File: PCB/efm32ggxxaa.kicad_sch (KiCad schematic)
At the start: 8 parts, among them U5 EFM32GG11B420F2048GQ100

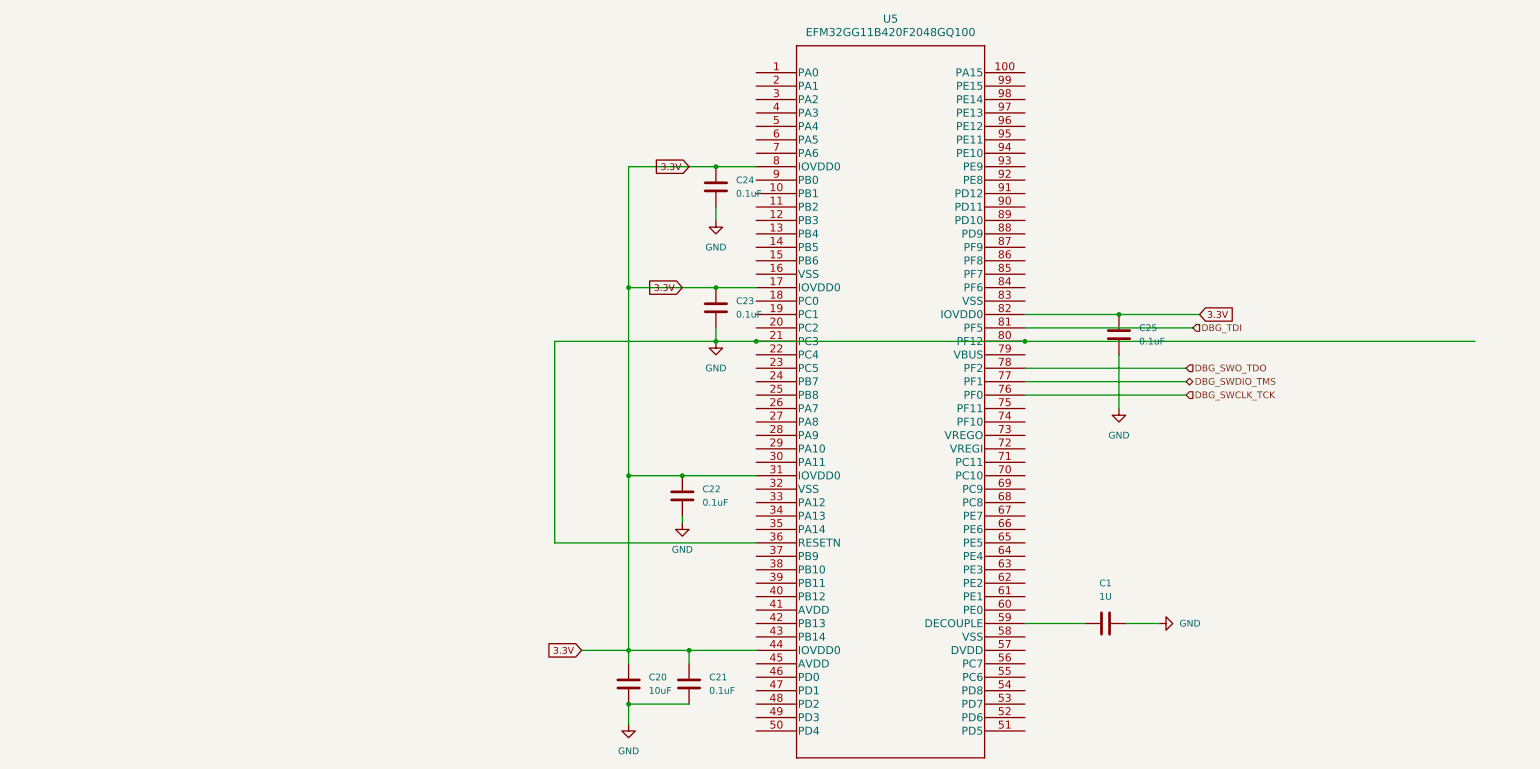
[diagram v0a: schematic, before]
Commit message: Create hierarchical labels for base QSPI out from MCU
Signed-off-by: Daniel Yang Hansen <daniel.yang.hansen@gmail.com>
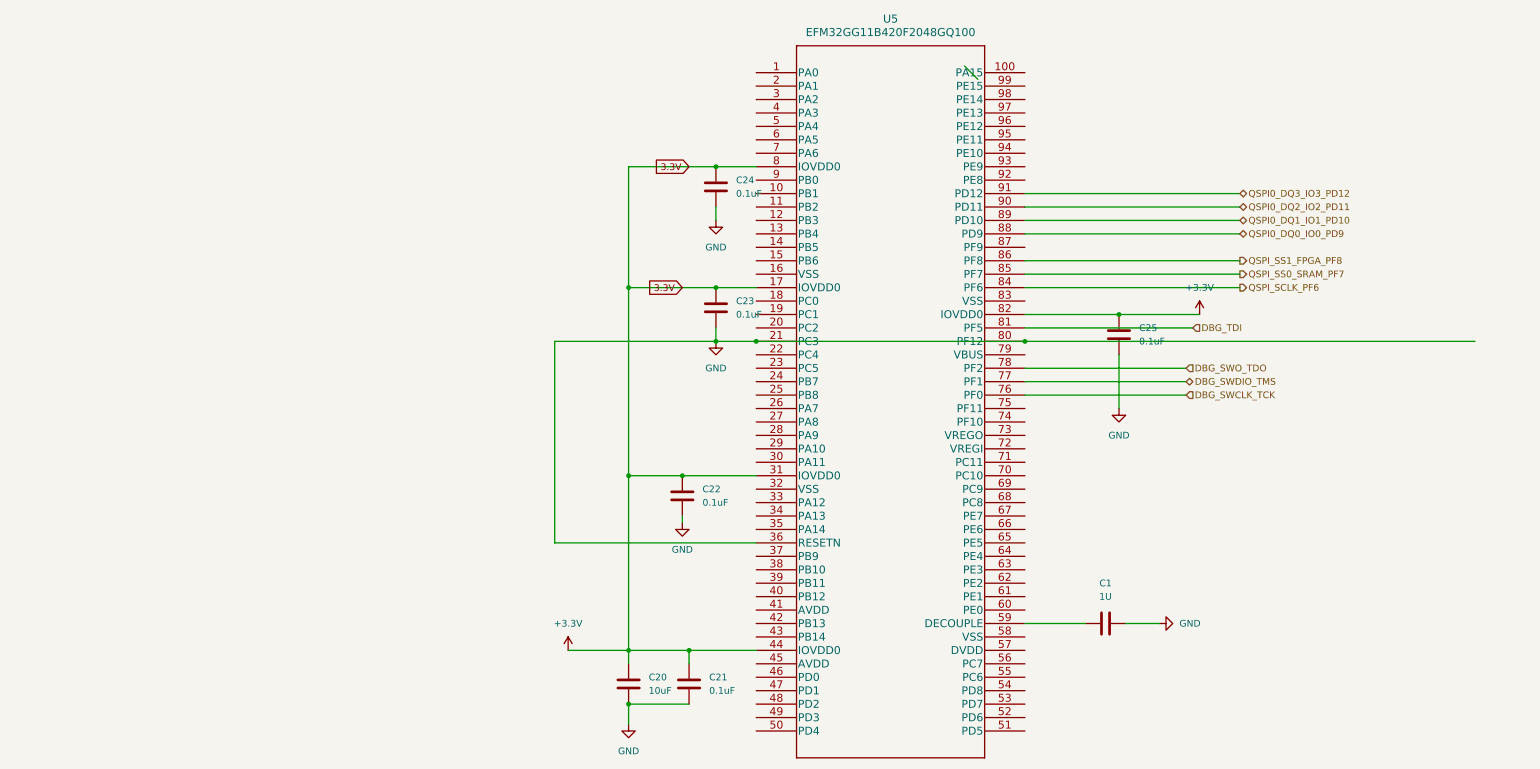
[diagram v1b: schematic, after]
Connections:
- net QSPI_SCLK_PF6: now reaches U5.84 (PF6)
- net QSPI_SS0_SRAM_PF7: now reaches U5.85 (PF7)
- net QSPI_SS1_FPGA_PF8: now reaches U5.86 (PF8)
- net QSPI0_DQ0_IO0_PD9: now reaches U5.88 (PD9)
- net QSPI0_DQ1_IO1_PD10: now reaches U5.89 (PD10)
- net QSPI0_DQ2_IO2_PD11: now reaches U5.90 (PD11)
- net QSPI0_DQ3_IO3_PD12: now reaches U5.91 (PD12)
- net 3.3V renamed +3.3V
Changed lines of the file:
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@@
   (junction (at 123.19 82.55) (diameter 0) (color 0 0 0 0)
   )
+  (bus_entry (at 162.56 30.48) (size 2.54 2.54)
+    (stroke (width 0) (type default))
+  )
+  (wire (pts (xy 214.63 62.23) (xy 173.99 62.23))
+    (stroke (width 0) (type default))
+  )
   (wire (pts (xy 85.09 120.65) (xy 123.19 120.65))
     (stroke (width 0) (type default))
   )
-  (wire (pts (xy 90.17 140.97) (xy 99.06 140.97))
+  (wire (pts (xy 87.63 140.97) (xy 99.06 140.97))
     (stroke (width 0) (type default))
   )
@@
     (stroke (width 0) (type default))
   )
+  (wire (pts (xy 214.63 69.85) (xy 173.99 69.85))
+    (stroke (width 0) (type default))
+  )
   (wire (pts (xy 99.06 49.53) (xy 99.06 72.39))
     (stroke (width 0) (type default))
   )
+  (wire (pts (xy 214.63 57.15) (xy 173.99 57.15))
+    (stroke (width 0) (type default))
+  )
   (wire (pts (xy 173.99 92.71) (xy 204.47 92.71))
     (stroke (width 0) (type default))
@@
     (stroke (width 0) (type default))
   )
+  (wire (pts (xy 214.63 72.39) (xy 173.99 72.39))
+    (stroke (width 0) (type default))
+  )
+  (wire (pts (xy 214.63 67.31) (xy 173.99 67.31))
+    (stroke (width 0) (type default))
+  )
+  (wire (pts (xy 214.63 59.69) (xy 173.99 59.69))
+    (stroke (width 0) (type default))
+  )
   (wire (pts (xy 85.09 82.55) (xy 85.09 120.65))
     (stroke (width 0) (type default))
@@
     (stroke (width 0) (type default))
   )
+  (wire (pts (xy 214.63 54.61) (xy 173.99 54.61))
+    (stroke (width 0) (type default))
+  )
   (wire (pts (xy 109.22 107.95) (xy 123.19 107.95))
     (stroke (width 0) (type default))
@@
   (wire (pts (xy 99.06 107.95) (xy 109.22 107.95))
     (stroke (width 0) (type default))
-  )
-  (global_label "3.3V" (shape input) (at 90.17 140.97 180) (fields_autoplaced)
-    (effects (font (size 1.27 1.27)) (justify right))
-    (property "Intersheetrefs" "${INTERSHEET_REFS}" (at 83.0724 140.97 0)
-      (effects (font (size 1.27 1.27)) (justify right) hide)
-    )
   )
   (global_label "3.3V" (shape input) (at 110.49 49.53 180) (fields_autoplaced)
@@
     )
   )
-  (global_label "3.3V" (shape input) (at 207.01 77.47 0) (fields_autoplaced)
-    (effects (font (size 1.27 1.27)) (justify left))
-    (property "Intersheetrefs" "${INTERSHEET_REFS}" (at 214.1076 77.47 0)
-      (effects (font (size 1.27 1.27)) (justify left) hide)
-    )
-  )
   (global_label "3.3V" (shape input) (at 109.22 72.39 180) (fields_autoplaced)
     (effects (font (size 1.27 1.27)) (justify right))
@@
     )
   )
+  (hierarchical_label "QSPI0_DQ3_IO3_PD12" (shape bidirectional) (at 214.63 54.61 0) (fields_autoplaced)
+    (effects (font (size 1.27 1.27)) (justify left))
+  )
   (hierarchical_label "DBG_TDI" (shape input) (at 205.74 80.01 0) (fields_autoplaced)
     (effects (font (size 1.27 1.27)) (justify left))
   )
+  (hierarchical_label "QSPI_SS0_SRAM_PF7" (shape output) (at 214.63 69.85 0) (fields_autoplaced)
+    (effects (font (size 1.27 1.27)) (justify left))
+  )
+  (hierarchical_label "QSPI0_DQ1_IO1_PD10" (shape bidirectional) (at 214.63 59.69 0) (fields_autoplaced)
+    (effects (font (size 1.27 1.27)) (justify left))
+  )
   (hierarchical_label "DBG_SWO_TDO" (shape input) (at 204.47 87.63 0) (fields_autoplaced)
     (effects (font (size 1.27 1.27)) (justify left))
@@
     (effects (font (size 1.27 1.27)) (justify left))
   )
+  (hierarchical_label "QSPI_SCLK_PF6" (shape output) (at 214.63 72.39 0) (fields_autoplaced)
+    (effects (font (size 1.27 1.27)) (justify left))
+  )
+  (hierarchical_label "QSPI0_DQ2_IO2_PD11" (shape bidirectional) (at 214.63 57.15 0) (fields_autoplaced)
+    (effects (font (size 1.27 1.27)) (justify left))
+  )
+  (hierarchical_label "QSPI0_DQ0_IO0_PD9" (shape bidirectional) (at 214.63 62.23 0) (fields_autoplaced)
+    (effects (font (size 1.27 1.27)) (justify left))
+  )
   (hierarchical_label "DBG_SWCLK_TCK" (shape input) (at 204.47 92.71 0) (fields_autoplaced)
+    (effects (font (size 1.27 1.27)) (justify left))
+  )
+  (hierarchical_label "QSPI_SS1_FPGA_PF8" (shape output) (at 214.63 67.31 0) (fields_autoplaced)
     (effects (font (size 1.27 1.27)) (justify left))
   )
@@
     )
   )
+  (symbol (lib_id "power:+3.3V") (at 87.63 140.97 0) (unit 1)
+    (in_bom yes) (on_board yes) (dnp no) (fields_autoplaced)
+    (property "Reference" "#PWR016" (at 87.63 144.78 0)
+      (effects (font (size 1.27 1.27)) hide)
+    )
+    (property "Value" "+3.3V" (at 87.63 135.89 0)
+      (effects (font (size 1.27 1.27)))
+    )
+    (property "Footprint" "" (at 87.63 140.97 0)
+      (effects (font (size 1.27 1.27)) hide)
+    )
+    (property "Datasheet" "" (at 87.63 140.97 0)
+      (effects (font (size 1.27 1.27)) hide)
+    )
+    (pin "1")
+    (instances
+      (project "RayTracingPCB"
+        (path "/e9047d94-28be-4266-894b-6ee25ef088bd/f9a74965-bde5-47a2-9f66-243cb6fc0f53"
+          (reference "#PWR016") (unit 1)
+        )
+      )
+    )
+  )
   (symbol (lib_id "Device:C") (at 115.57 76.2 0) (unit 1)
     (in_bom yes) (on_board yes) (dnp no) (fields_autoplaced)
@@
         )
       )
+    )
+  )
+  (symbol (lib_id "power:+3.3V") (at 207.01 77.47 0) (unit 1)
+    (in_bom yes) (on_board yes) (dnp no) (fields_autoplaced)
+    (property "Reference" "#PWR017" (at 207.01 81.28 0)
+      (effects (font (size 1.27 1.27)) hide)
+    )
+    (property "Value" "+3.3V" (at 207.01 72.39 0)
+      (effects (font (size 1.27 1.27)))
+    )
+    (property "Footprint" "" (at 207.01 77.47 0)
+      (effects (font (size 1.27 1.27)) hide)
+    )
+    (property "Datasheet" "" (at 207.01 77.47 0)
+      (effects (font (size 1.27 1.27)) hide)
+    )
+    (pin "1")
+    (instances
+      (project "RayTracingPCB"
+        (path "/e9047d94-28be-4266-894b-6ee25ef088bd/f9a74965-bde5-47a2-9f66-243cb6fc0f53"
+          (reference "#PWR017") (unit 1)
+        )
+      )

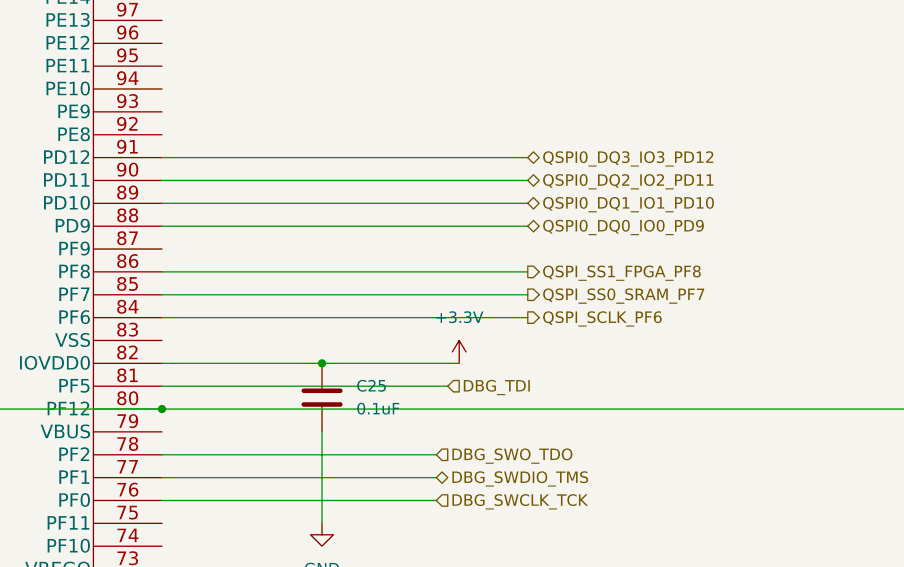
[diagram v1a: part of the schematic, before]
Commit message: Trace QSPI for MCU Master (#7), slaves unconnected
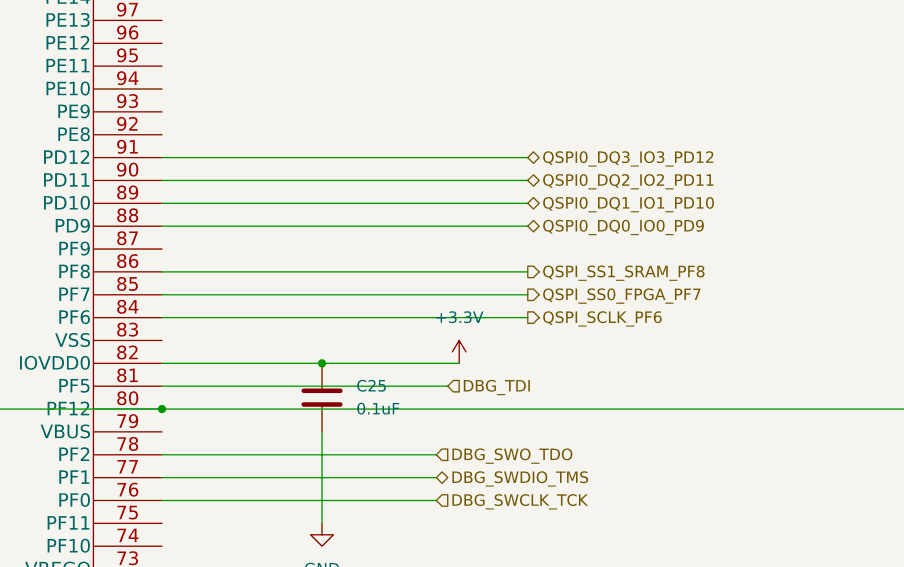
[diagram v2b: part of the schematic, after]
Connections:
- net QSPI_SS0_SRAM_PF7 renamed QSPI_SS0_FPGA_PF7
- net QSPI_SS1_FPGA_PF8 renamed QSPI_SS1_SRAM_PF8
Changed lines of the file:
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@@
-    (stroke (width 0) (type default))
-  )
-  (wire (pts (xy 214.63 69.85) (xy 173.99 69.85))
     (stroke (width 0) (type default))
   )
@@
     (stroke (width 0) (type default))
   )
-  (wire (pts (xy 214.63 67.31) (xy 173.99 67.31))
-    (stroke (width 0) (type default))
-  )
   (wire (pts (xy 214.63 59.69) (xy 173.99 59.69))
     (stroke (width 0) (type default))
   )
   (wire (pts (xy 85.09 82.55) (xy 85.09 120.65))
+    (stroke (width 0) (type default))
+  )
+  (wire (pts (xy 173.99 67.31) (xy 214.63 67.31))
     (stroke (width 0) (type default))
   )
@@
     (stroke (width 0) (type default))
   )
+  (wire (pts (xy 173.99 69.85) (xy 214.63 69.85))
+    (stroke (width 0) (type default))
+  )
   (wire (pts (xy 115.57 57.15) (xy 115.57 59.69))
     (stroke (width 0) (type default))
@@
     (effects (font (size 1.27 1.27)) (justify left))
   )
-  (hierarchical_label "QSPI_SS0_SRAM_PF7" (shape output) (at 214.63 69.85 0) (fields_autoplaced)
+  (hierarchical_label "QSPI_SS1_SRAM_PF8" (shape output) (at 214.63 67.31 0) (fields_autoplaced)
     (effects (font (size 1.27 1.27)) (justify left))
   )
@@
     (effects (font (size 1.27 1.27)) (justify left))
   )
-  (hierarchical_label "QSPI_SS1_FPGA_PF8" (shape output) (at 214.63 67.31 0) (fields_autoplaced)
+  (hierarchical_label "QSPI_SS0_FPGA_PF7" (shape output) (at 214.63 69.85 0) (fields_autoplaced)
     (effects (font (size 1.27 1.27)) (justify left))
   )

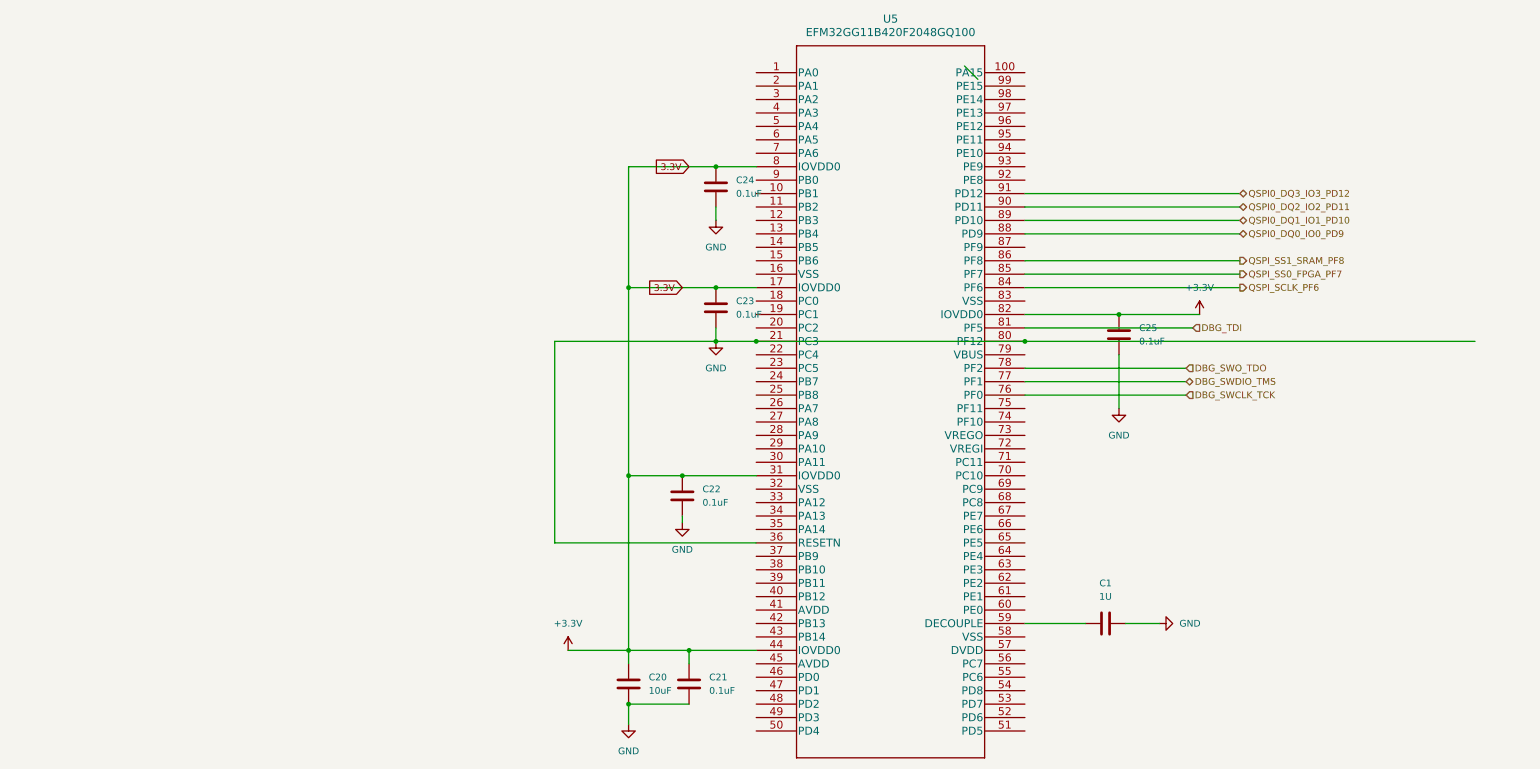
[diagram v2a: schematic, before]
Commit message: Add Local Library Component and Implement USB Mini Connector
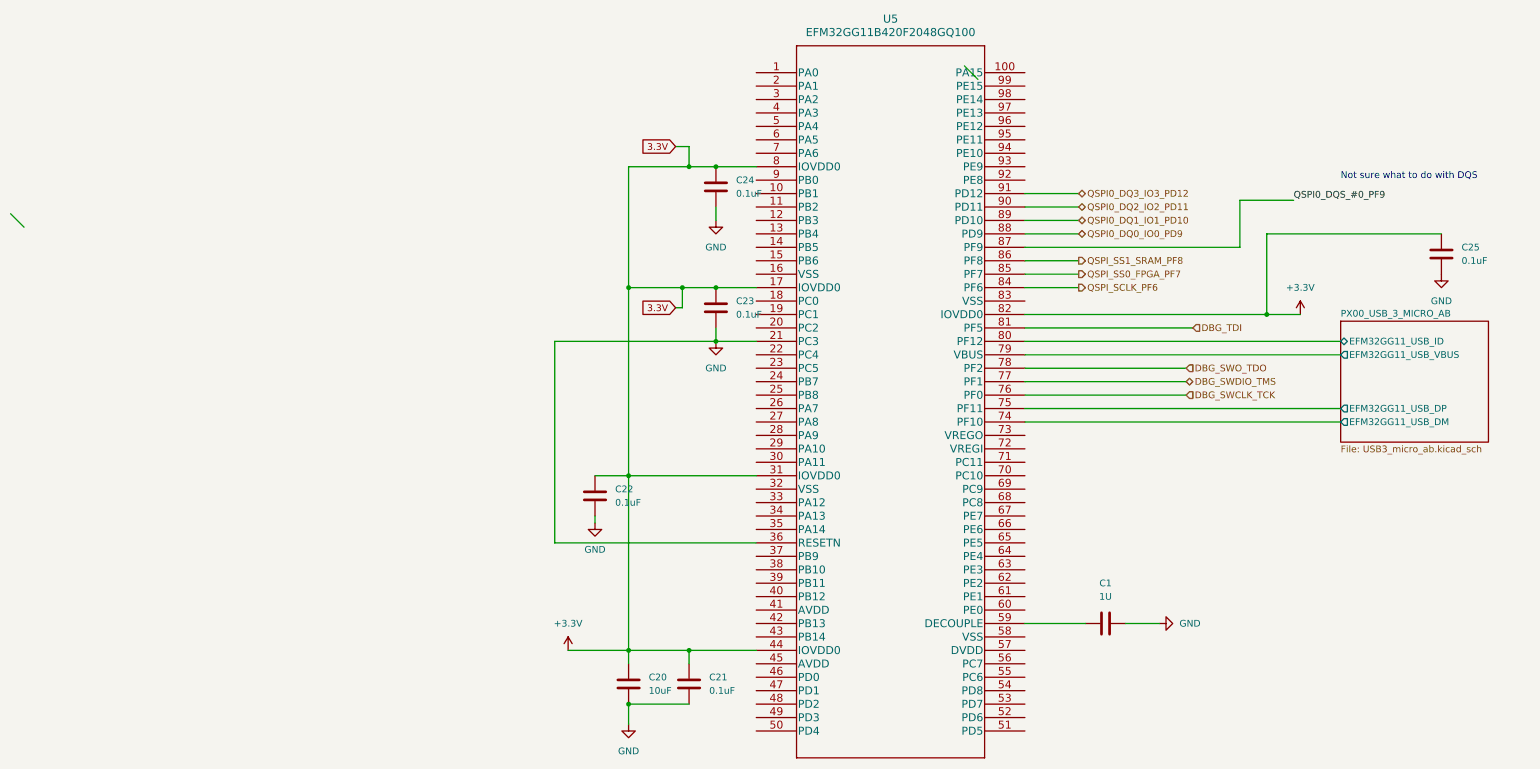
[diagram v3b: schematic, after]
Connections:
- net GND: no longer U5.80 (PF12)
- net PX00_USB_3_MICRO_AB/EFM32GG11_USB_DM: now reaches U5.74 (PF10)
- net PX00_USB_3_MICRO_AB/EFM32GG11_USB_DP: now reaches U5.75 (PF11)
- net PX00_USB_3_MICRO_AB/EFM32GG11_USB_VBUS: now reaches U5.79 (VBUS)
- net QSPI0_DQS_#0_PF9: now reaches U5.87 (PF9)
- new net PX00_USB_3_MICRO_AB/EFM32GG11_USB_ID: U5.80 (PF12)
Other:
- added sheet PX00_USB_3_MICRO_AB (USB3_micro_ab.kicad_sch)
- note added: "Not sure what to do with DQS"
- moved on the sheet: C22, C25
